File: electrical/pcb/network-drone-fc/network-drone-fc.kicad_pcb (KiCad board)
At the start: 4 copper layers, 36 x 39 mm, 83 parts, among them J1 U.FL-R-SMT-1, J2 TYPE-C 16PIN 2MD, J3 U.FL GPS, J4 ESC, J5 I2C port, J7 Charging board, U1 ESP32-S3FN8, U2 USBLC6-2SC6, U3 AP63205WU-7, U4 TLV75733PDBVR, U5 TPS7A2033PDBVR, U6 ICM-42688-P, U7 BMP581, U8 MAX-M10S, X1 Q22FA12800101

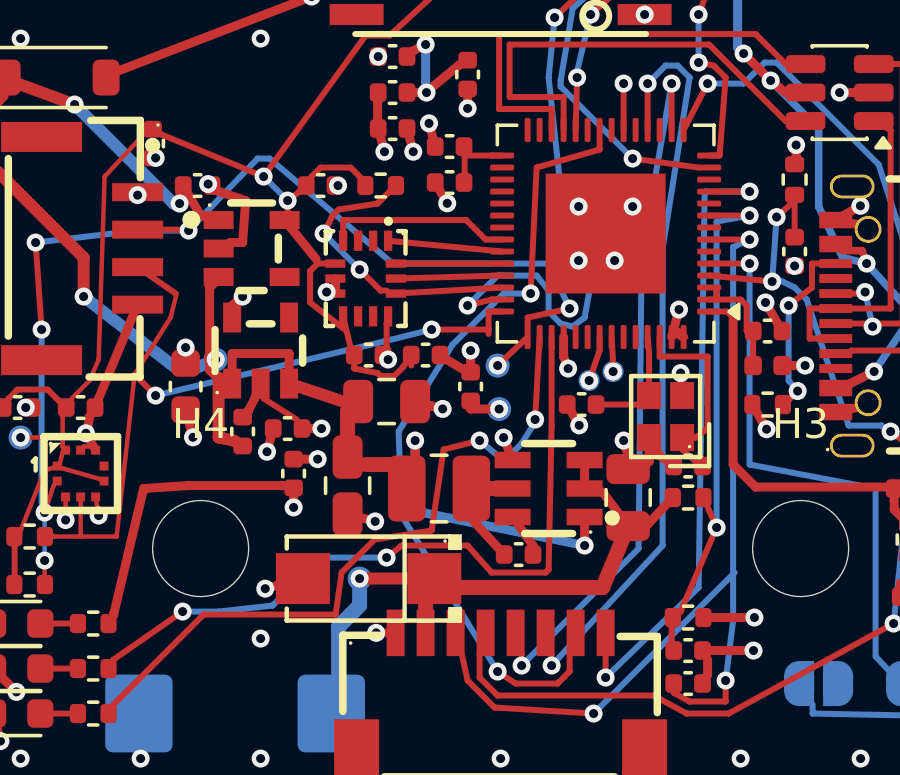
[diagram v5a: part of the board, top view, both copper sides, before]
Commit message: PCB: U4 in the WSON-6 footprint with a via under its pad; C16 as a 1206 with the crystal moved up 0.6 mm; DRC clean
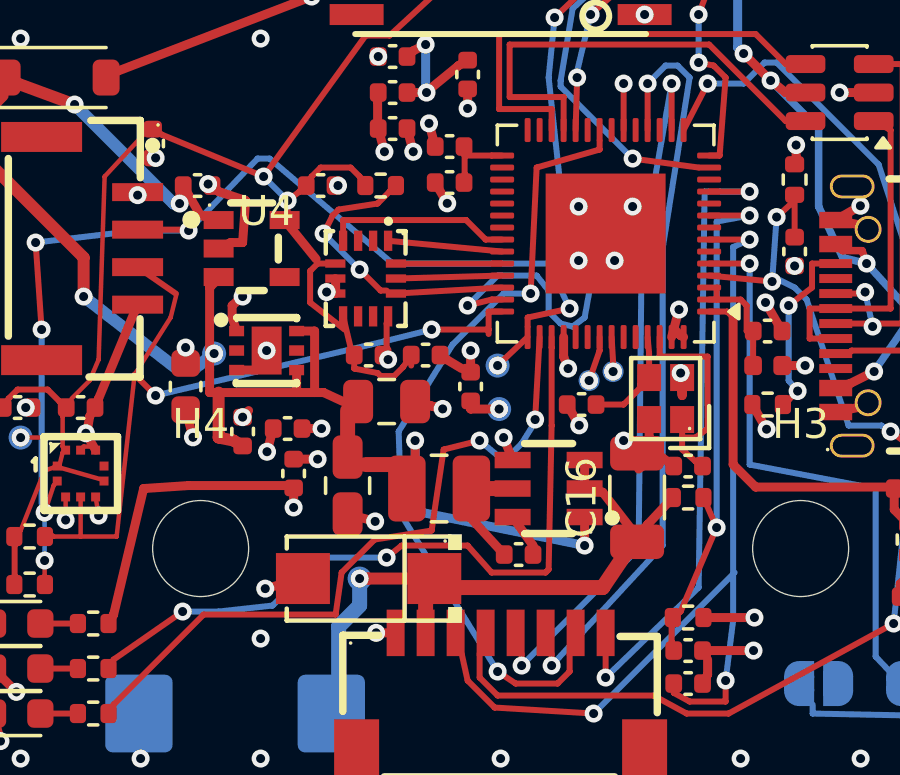
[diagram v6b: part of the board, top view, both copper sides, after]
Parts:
- C16: footprint C_0805_2012Metric -> C_1206_3216Metric
- U4: value TLV75733PDBVR -> TLV75733PDRVR; footprint SOT-23-5_L2.9-W1.6-P0.95-LS2.8-BL -> TDFN-6_L2.0-W2.0-P0.65-TL-EP
- moved X1 0.60 mm to (105.5, 105.0)
- moved C16 0.30 mm to (104.5, 108.3)
- moved TP4 0.21 mm to (90.5, 103.5)
- moved U4 0.20 mm to (92.2, 103.4)
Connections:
- U4 pad 1: +5V -> +3V3
- U4 pad 2: GND -> (no net)
- U4 pad 3: +5V -> GND
- U4 pad 4: (no net) -> +5V
- U4 pad 5: +3V3 -> (no net)
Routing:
- net +5V: track 48.4 -> 49.7 mm
- net GND: track 66.9 -> 66.2 mm, vias 80 -> 82
- net XTAL_P: track 6.88 -> 7.48 mm

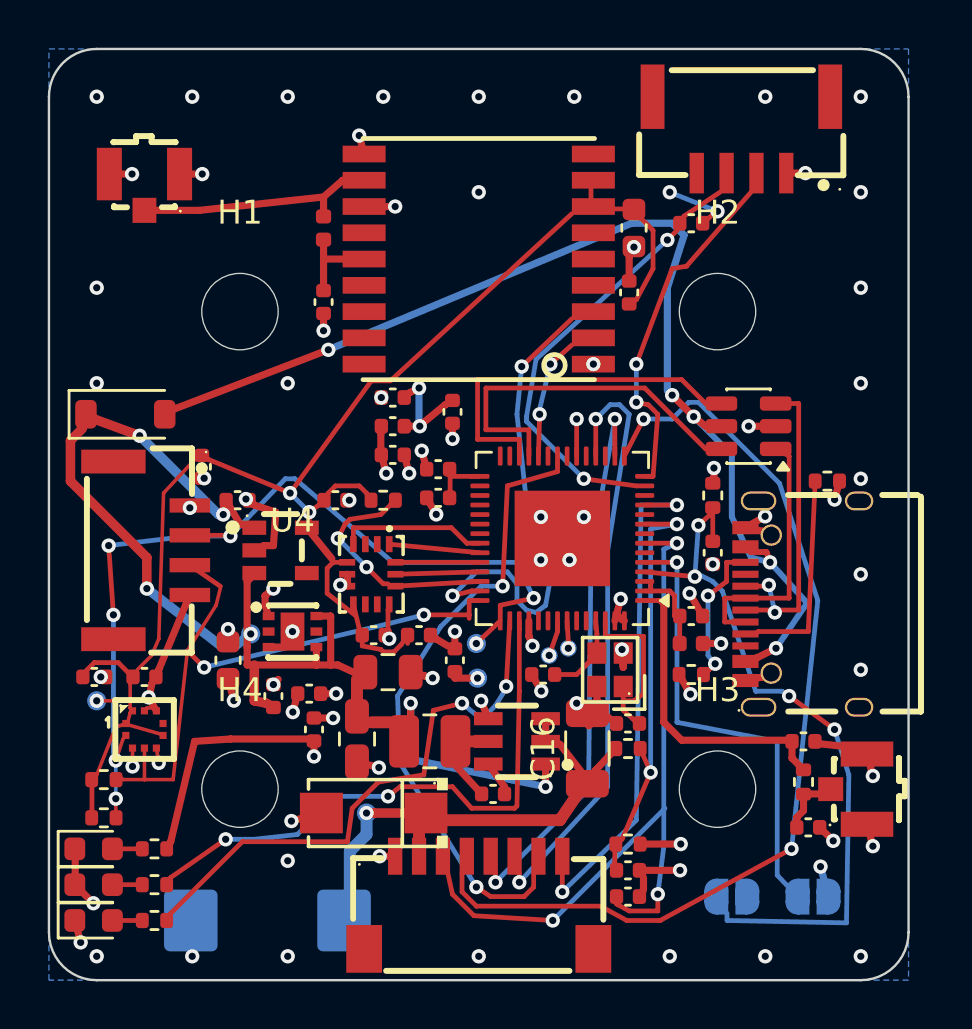
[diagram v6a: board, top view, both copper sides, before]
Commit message: PCB: second optimisation pass; I2C_SCL 38 to 33 mm and 7 to 4 vias, ESC_CUR and MOTOR4 shortened, RESET pair one via fewer; 156 vias, DRC clean
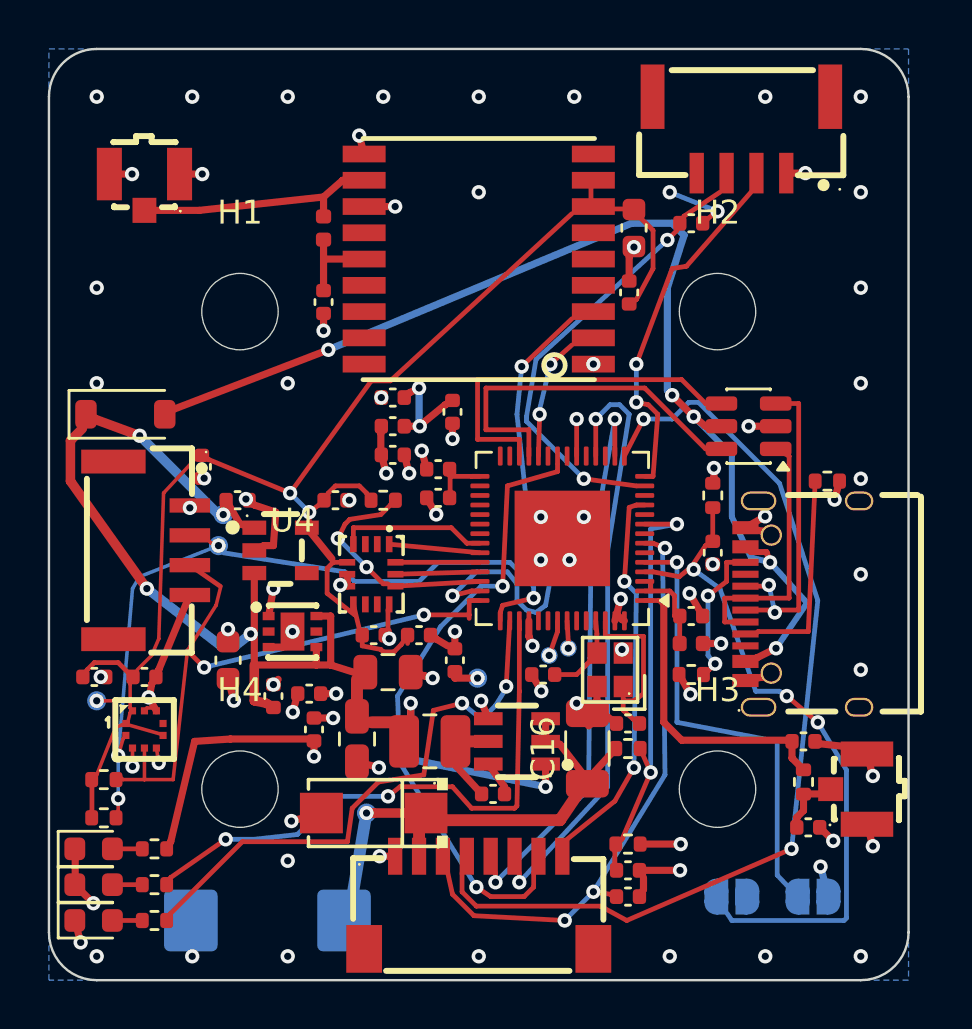
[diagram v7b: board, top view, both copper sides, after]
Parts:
- moved TP13 11.6 mm to (89.1, 99.8)
- moved TP4 5.13 mm to (89.3, 98.5)
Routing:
- net ESC_CUR: track 31.4 -> 24.9 mm
- net I2C_SCL: track 38.1 -> 31.6 mm, vias 7 -> 4
- net MOTOR4: track 21.9 -> 16.0 mm
- net Net-(JP1-B): track 29.7 -> 27.8 mm, vias 4 -> 3
- net GND: track 66.2 -> 65.0 mm
- net +5V: track 49.7 -> 48.9 mm

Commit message: PCB: second straightening pass; corner redraws and 111 stubs hidden inside pads removed (544 to 432 segments), DRC clean
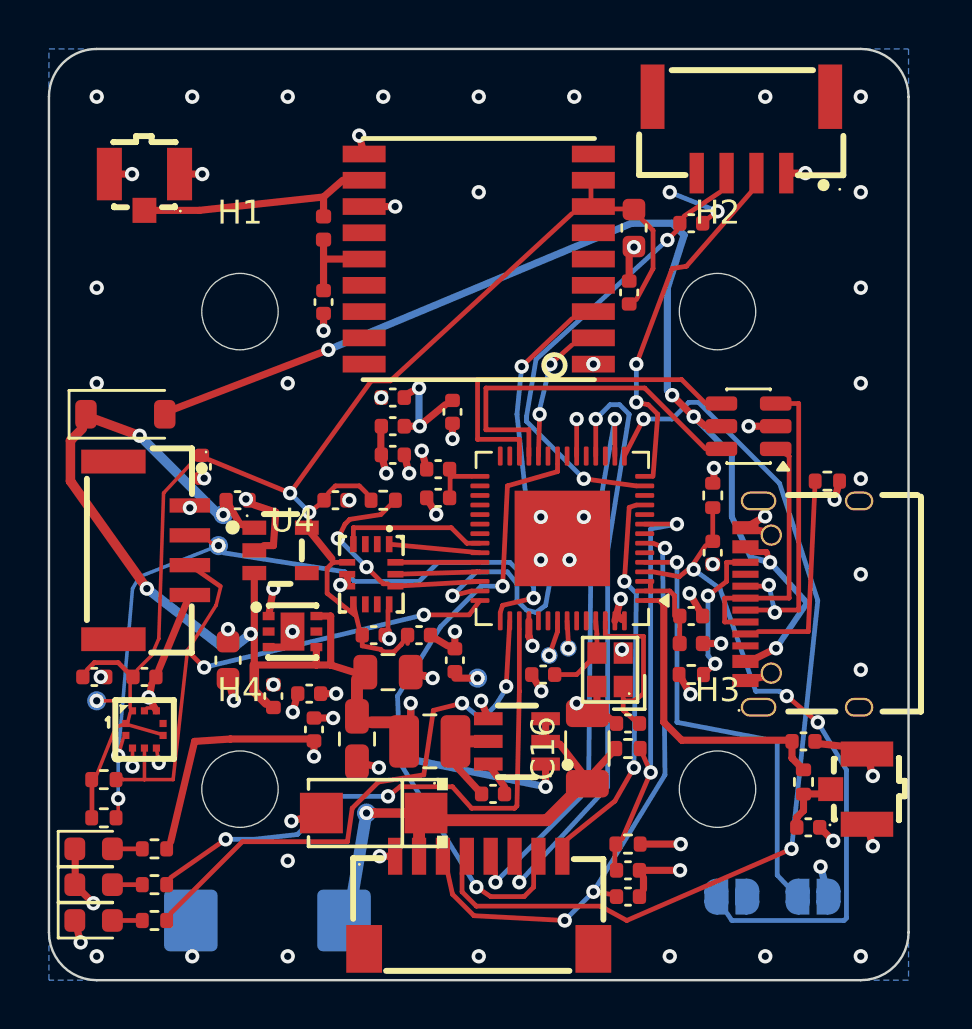
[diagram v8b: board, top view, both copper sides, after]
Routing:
- net GND: track 65.0 -> 55.3 mm
- net +3V3_SENS: track 64.4 -> 58.1 mm
- net VBUS: track 48.0 -> 46.1 mm
- net +3V3: track 21.5 -> 20.2 mm
- net Net-(U1-VDD_SPI): track 2.75 -> 1.50 mm
- net +5V: track 48.9 -> 47.7 mm
- net VBAT: track 21.3 -> 20.1 mm
- net Net-(JP1-B): track 27.8 -> 26.7 mm
- net VBAT_SENSE: track 18.2 -> 17.3 mm
- net Net-(J3-SIG): track 10.3 -> 9.41 mm
- net I2C_SCL: track 31.6 -> 30.8 mm
- net Net-(U8-VCC_RF): track 3.84 -> 3.14 mm
- net Green: track 24.4 -> 23.7 mm
- net AUX_ADC: track 18.7 -> 18.0 mm
- net I2C_SDA: track 27.4 -> 26.7 mm
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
